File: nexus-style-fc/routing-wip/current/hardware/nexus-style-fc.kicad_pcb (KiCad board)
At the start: 6 copper layers, 22.4 x 33.1 mm, 88 parts, among them J1 Header child board, J2 DSM (UART1), J3 A-CRSF (UART4), J4 C (UART3), J5 B (UART6), J6 USB-C vertical, SW1 BOOT, U1 STM32F722RET6, U10 TPS70933DBVR, U11 SRV05-4, U12 SRV05-4, U13 SRV05-4, U14 TPS629210DRLR, U15 SRV05-4, U2 ICM-42688-P, U3 DPS368XTSA1, U4 W25N01GVZEIG, U5 TPS62130RGTR, U7 USBLC6-2SC6, U9 TPS2116DRLR, Y1 8MHz 20pF

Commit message: Nexus WIP: publish r62 input-cap star with zero native errors
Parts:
- added C31: 22uF, NexusFC:C_0805_2012Metric_Samsung_CL21_MinLand, B.Cu at (105.8, 126.3)
- C27: value 4.7uF -> 22uF; footprint Capacitor_SMD:C_0603_1608Metric -> NexusFC:C_0805_2012Metric_Samsung_CL21_MinLand
- moved D5 0.40 mm to (102.3, 126.2)
- moved C27 0.26 mm to (101.9, 124.3)
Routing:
- net VSYS: track 44.1 -> 64.5 mm, vias 4 -> 7
- net GND: track 225.4 -> 232.0 mm, vias 76 -> 77
- net DSM_TX: track 37.5 -> 41.0 mm
- net VX: track 100.1 -> 101.6 mm
- net SCONF: track 7.86 -> 8.06 mm, vias 2 -> 3

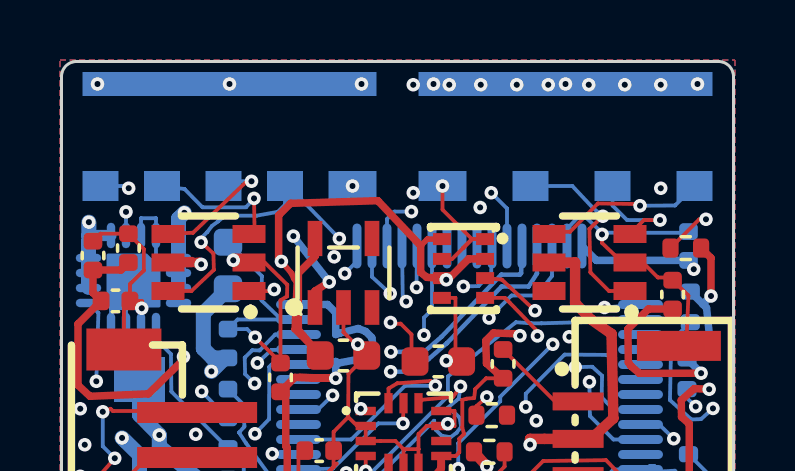
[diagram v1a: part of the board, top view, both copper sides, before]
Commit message: Nexus WIP: integrate zero-error header interface and restore signal returns
Keep current candidate atomic with matching main/child source, native evidence and WIP exports. Physical assembly, manufacturing process and electrical qualification remain open. No unrelated project changes.
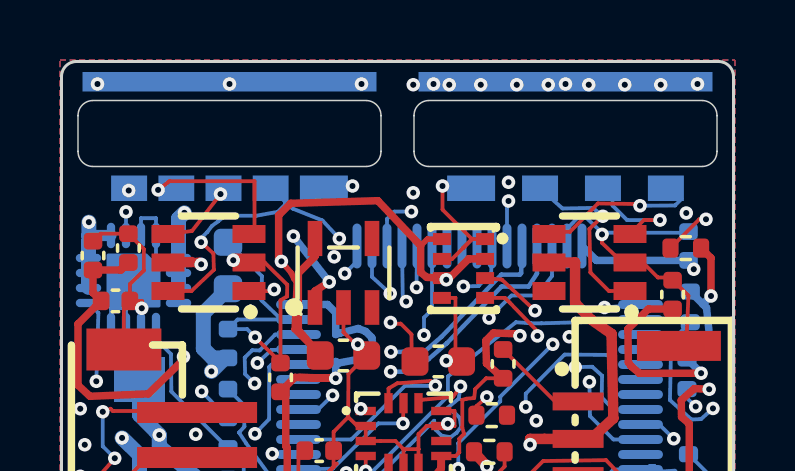
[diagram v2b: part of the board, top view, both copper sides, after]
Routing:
- net VX: track 101.6 -> 97.0 mm
- net RPM: track 20.5 -> 24.4 mm
- net TAIL: track 23.9 -> 25.0 mm
- net SBUS: track 20.6 -> 19.6 mm
- net ESC: track 23.4 -> 24.3 mm
- net S1: track 16.9 -> 16.3 mm
- net DSM_DATA: track 61.6 -> 62.2 mm

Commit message: Nexus WIP: source-consistent assembly markings and release-gate evidence
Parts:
- D1: footprint NexusFC:LED0603-RD_GREEN -> NexusFC:LED0603-RD_GREEN__NexusMain_D1
- D2: footprint NexusFC:LED0603-RD_RED -> NexusFC:LED0603-RD_RED__NexusMain_D2
- D3: footprint NexusFC:LED0603-RD_BLUE -> NexusFC:LED0603-RD_BLUE__NexusMain_D3
- J4: footprint NexusFC:CONN-SMD_4P-P1.25_BM04B-GHS-TBT-LF-SN -> NexusFC:CONN-SMD_4P-P1.25_BM04B-GHS-TBT-LF-SN__NexusMain_J4
- J6: footprint NexusFC:USB-C-SMD_TYPE-C-31-D-06 -> NexusFC:USB-C-SMD_TYPE-C-31-D-06__NexusMain_J6
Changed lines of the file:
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@@
 		)
 	)
-	(footprint "NexusFC:USB-C-SMD_TYPE-C-31-D-06"
+	(footprint "NexusFC:USB-C-SMD_TYPE-C-31-D-06__NexusMain_J6"
 		(layer "F.Cu")
 		(at 108.4 129.8)
@@
 		(fp_line
 			(start 4.5 -1.6)
+			(end 4.5 -0.925)
+			(stroke
+				(width 0.25)
+				(type solid)
+			)
+			(layer "F.SilkS")
+		)
+		(fp_line
+			(start 4.5 0.925)
 			(end 4.5 1.6)
 			(stroke
@@
 			)
 		)
-		(attr through_hole)
+		(attr smd)
 		(duplicate_pad_numbers_are_jumpers no)
 		(fp_line
@@
 		(embedded_fonts no)
 	)
-	(footprint "NexusFC:LED0603-RD_BLUE"
+	(footprint "NexusFC:LED0603-RD_BLUE__NexusMain_D3"
 		(layer "F.Cu")
 		(at 111.2 125.1)
@@
 		)
 		(fp_circle
-			(center -0.8 0.4)
-			(end -0.77 0.4)
+			(center -0.8 1.15)
+			(end -0.725 1.15)
 			(stroke
-				(width 0.06)
+				(width 0.15)
 				(type solid)
 			)
-			(fill no)
+			(fill yes)
 			(layer "F.SilkS")
 		)
@@
 		)
 	)
-	(footprint "NexusFC:LED0603-RD_RED"
+	(footprint "NexusFC:LED0603-RD_RED__NexusMain_D2"
 		(layer "F.Cu")
 		(at 114.4 125.1)
@@
 		)
 		(fp_circle
-			(center -0.8 0.4)
-			(end -0.77 0.4)
+			(center -0.8 1.15)
+			(end -0.725 1.15)
 			(stroke
-				(width 0.06)
+				(width 0.15)
 				(type solid)
 			)
-			(fill no)
+			(fill yes)
 			(layer "F.SilkS")
 		)
@@
 		)
 	)
-	(footprint "NexusFC:CONN-SMD_4P-P1.25_BM04B-GHS-TBT-LF-SN"
+	(footprint "NexusFC:CONN-SMD_4P-P1.25_BM04B-GHS-TBT-LF-SN__NexusMain_J4"
 		(layer "F.Cu")
 		(at 106 121)
@@
 		(fp_line
 			(start -4.57 -1.78)
-			(end -4.57 3.43)
+			(end -4.57 0.475)
 			(stroke
 				(width 0.25)
@@
 		)
 		(fp_line
+			(start -4.57 2.325)
+			(end -4.57 3.43)
+			(stroke
+				(width 0.25)
+				(type solid)
+			)
+			(layer "F.SilkS")
+		)
+		(fp_line
 			(start -4.57 3.43)
 			(end 4.57 3.43)
@@
 		)
 	)
-	(footprint "NexusFC:LED0603-RD_GREEN"
+	(footprint "NexusFC:LED0603-RD_GREEN__NexusMain_D1"
 		(layer "F.Cu")
 		(at 108 125.1)
@@
 		)
 		(fp_circle
-			(center -0.8 0.4)
-			(end -0.77 0.4)
+			(center -0.8 1.15)
+			(end -0.725 1.15)
 			(stroke
-				(width 0.06)
+				(width 0.15)
 				(type solid)
 			)
-			(fill no)
+			(fill yes)
 			(layer "F.SilkS")
 		)
@@
 			)
 		)
-		(attr through_hole)
+		(attr smd)
 		(duplicate_pad_numbers_are_jumpers no)
 		(fp_line
@@
 			)
 		)
-		(attr through_hole)
+		(attr smd)
 		(duplicate_pad_numbers_are_jumpers no)
 		(fp_line
